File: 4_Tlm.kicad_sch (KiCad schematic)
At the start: 42 parts, among them J502 Conn_Coaxial, SW501 SW_Push, U501 W25Q128JVE, U502 RP2040, U503 Ra-08H

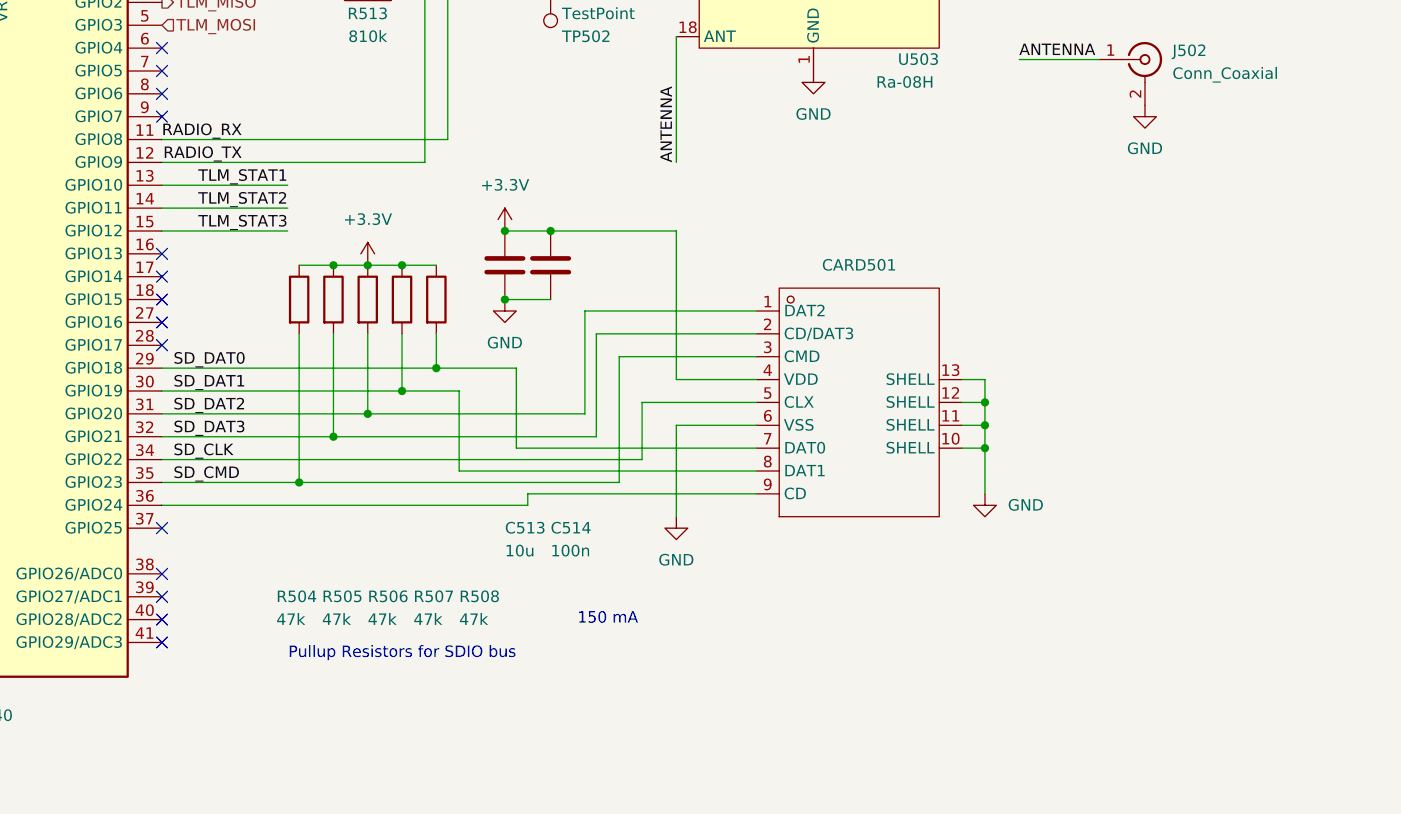
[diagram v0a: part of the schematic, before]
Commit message: Used a different microSD card slot symbol (The old one loooked bad)
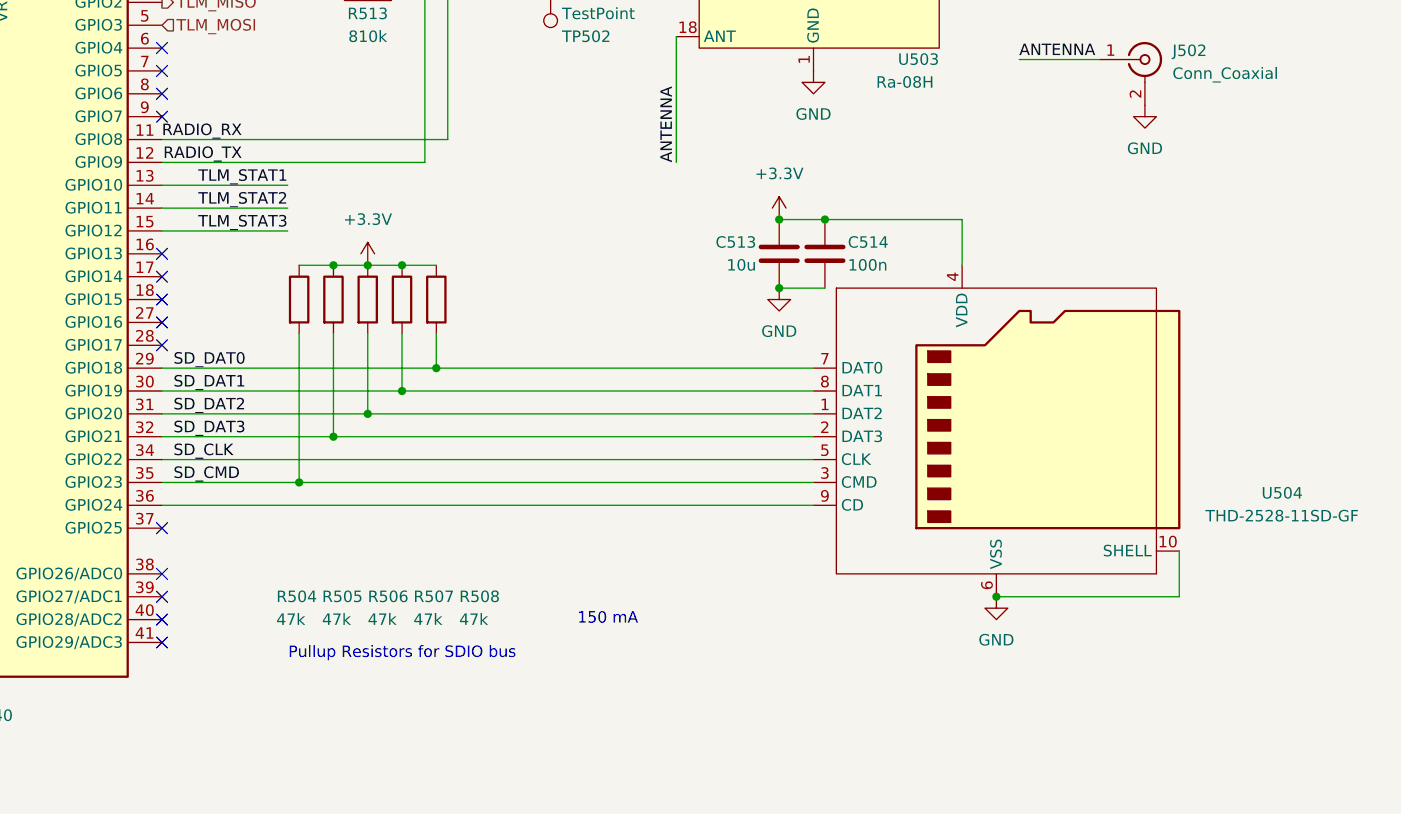
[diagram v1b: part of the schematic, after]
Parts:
- removed CARD501: (no value), Polaris:TF-SMD_THD2528-11SD-GF, symbol Polaris_symbols:THD2528-11SD-GF
- added U504: THD-2528-11SD-GF, Polaris:TF-SMD_THD2528-11SD-GF, symbol Polaris_symbols:MicroSD_THD2528-11SD-GF
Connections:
- net +3.3V: now also U504.4 (VDD)
- net GND: now also U504.10 (SHELL), U504.11 (SHELL), U504.12 (SHELL), U504.13 (SHELL), U504.6 (VSS)
- net SD_CLK: now also U504.5 (CLK)
- net SD_CMD: now also U504.3 (CMD)
- net SD_DAT0: now also U504.7 (DAT0)
- net SD_DAT1: now also U504.8 (DAT1)
- net SD_DAT2: now also U504.1 (DAT2)
- net SD_DAT3: now also U504.2 (DAT3)
- net at U502.36 (GPIO24): now also U504.9 (CD)
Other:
- moved on the sheet: C513, C514

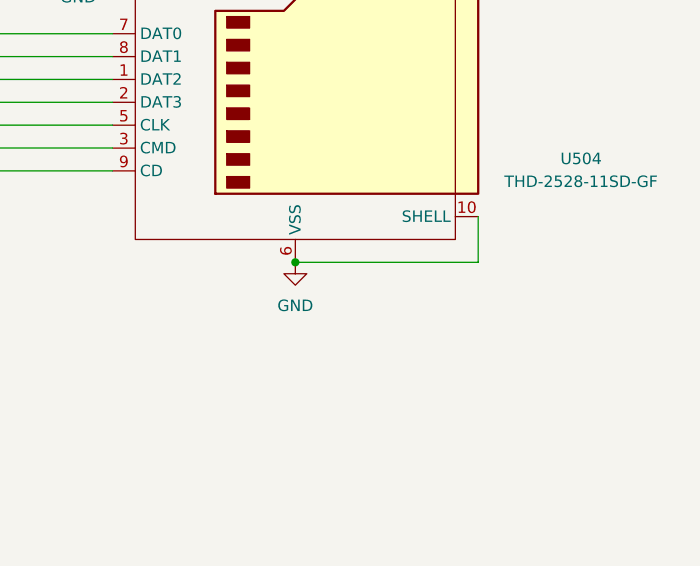
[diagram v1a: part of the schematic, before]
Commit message: Added hardware switch for active control Also added a coupling capacitor between receptacle shells and reference ground Added some more notes
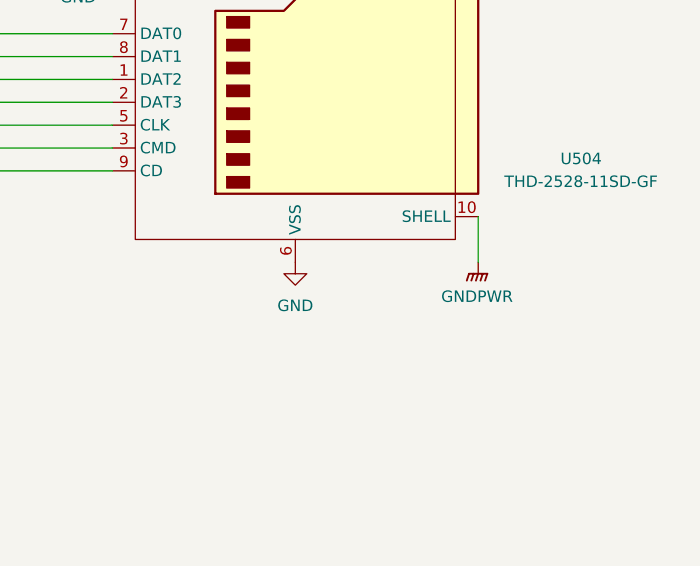
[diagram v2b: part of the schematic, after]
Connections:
- net GND: no longer U504.10 (SHELL), U504.11 (SHELL), U504.12 (SHELL), U504.13 (SHELL)
- new net GNDPWR: U504.10 (SHELL), U504.11 (SHELL), U504.12 (SHELL), U504.13 (SHELL)
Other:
- title: (none) -> Polaris/TLM
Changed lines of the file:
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@@
 	(generator_version "10.0")
 	(paper "A4")
+	(title_block
+		(title "Polaris/TLM")
+	)
 	(rectangle
 		(start 25.4 152.4)
@@
 	)
 	(junction
-		(at 251.46 158.75)
-		(diameter 0)
-		(color 0 0 0 0)
-	)
-	(junction
 		(at 171.45 60.96)
 		(diameter 0)
@@
 	(wire
 		(pts
-			(xy 271.78 153.67) (xy 271.78 158.75)
-		)
-		(stroke
-			(width 0)
-			(type default)
-		)
-	)
-	(wire
-		(pts
 			(xy 181.61 129.54) (xy 181.61 138.43)
 		)
@@
 	(wire
 		(pts
-			(xy 271.78 158.75) (xy 251.46 158.75)
+			(xy 232.41 116.84) (xy 247.65 116.84)
 		)
 		(stroke
@@
 	(wire
 		(pts
-			(xy 232.41 116.84) (xy 247.65 116.84)
+			(xy 177.8 129.54) (xy 177.8 140.97)
 		)
 		(stroke
@@
 	(wire
 		(pts
-			(xy 177.8 129.54) (xy 177.8 140.97)
+			(xy 171.45 60.96) (xy 179.07 60.96)
 		)
 		(stroke
@@
 	(wire
 		(pts
-			(xy 171.45 60.96) (xy 179.07 60.96)
+			(xy 95.25 110.49) (xy 100.33 110.49)
 		)
 		(stroke
@@
 	(wire
 		(pts
-			(xy 95.25 110.49) (xy 100.33 110.49)
+			(xy 177.8 140.97) (xy 231.14 140.97)
 		)
 		(stroke
@@
 	(wire
 		(pts
-			(xy 177.8 140.97) (xy 231.14 140.97)
+			(xy 53.34 130.81) (xy 107.95 130.81)
 		)
 		(stroke
@@
 	(wire
 		(pts
-			(xy 53.34 130.81) (xy 107.95 130.81)
+			(xy 53.34 133.35) (xy 107.95 133.35)
 		)
 		(stroke
@@
 	(wire
 		(pts
-			(xy 53.34 133.35) (xy 107.95 133.35)
+			(xy 271.78 153.67) (xy 271.78 158.75)
 		)
 		(stroke
@@
 					(unit 1)
 				)
+			)
+		)
+	)
+	(symbol
+		(lib_id "power:GNDPWR")
+		(at 271.78 158.75 0)
+		(unit 1)
+		(body_style 1)
+		(exclude_from_sim no)
+		(in_bom yes)
+		(on_board yes)
+		(in_pos_files yes)
+		(dnp no)
+		(fields_autoplaced yes)
+		(property "Reference" "#PWR0516"
+			(at 271.78 163.83 0)
+			(hide yes)
+			(show_name no)
+			(do_not_autoplace no)
+			(effects
+				(font
+					(size 1.27 1.27)
+				)
+			)
+		)
+		(property "Value" "GNDPWR"
+			(at 271.653 162.56 0)
+			(show_name no)
+			(do_not_autoplace no)
+			(effects
+				(font
+					(size 1.27 1.27)
+				)
+			)
+		)
+		(property "Footprint" ""
+			(at 271.78 160.02 0)
+			(hide yes)
+			(show_name no)
+			(do_not_autoplace no)
+			(effects
+				(font
+					(size 1.27 1.27)
+				)
+			)
+		)
+		(property "Datasheet" ""
+			(at 271.78 160.02 0)
+			(hide yes)
+			(show_name no)
+			(do_not_autoplace no)
+			(effects
+				(font
+					(size 1.27 1.27)
+				)
+			)
+		)
+		(property "Description" "Power symbol creates a global label with name \"GNDPWR\" , global ground"
+			(at 271.78 158.75 0)
+			(hide yes)
+			(show_name no)
+			(do_not_autoplace no)
+			(effects
+				(font
+					(size 1.27 1.27)
+				)
+			)
+		)
+		(pin "1"
+		)
+		(instances
+			(project "polaris"
+				(path "/cfb90e19-9fbe-47a1-a5ac-df522853d1d0/fe5e17e9-7440-4fbd-b2a1-319d9cc92848"
+					(reference "#PWR0516")
+					(unit 1)
+				)

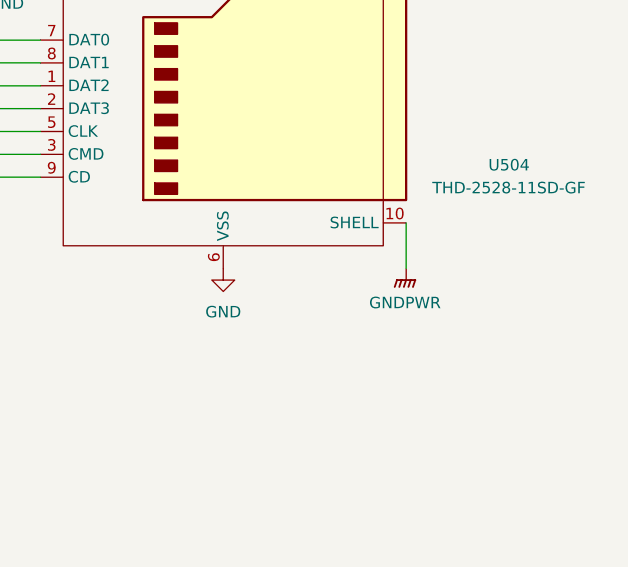
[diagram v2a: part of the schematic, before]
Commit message: Corrected grounding of shield pins in receptacles Also changed SHELL pin of microSD slot to Passive
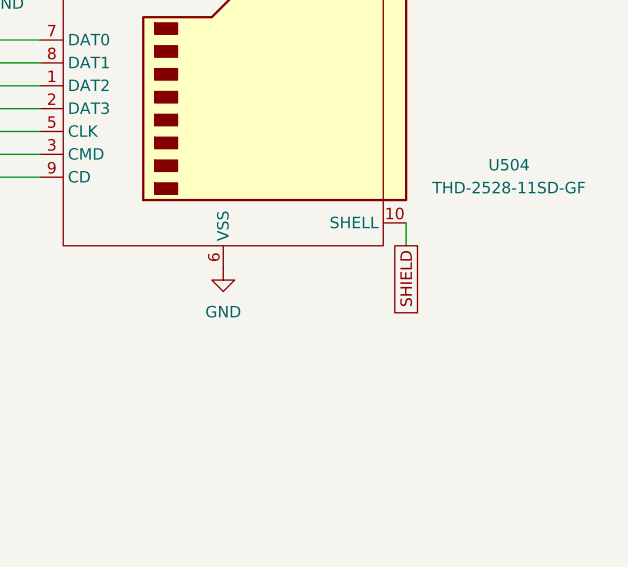
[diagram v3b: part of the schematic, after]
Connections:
- net GNDPWR renamed SHIELD
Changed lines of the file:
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@@
+	(wire
+		(pts
+			(xy 271.78 153.67) (xy 271.78 156.21)
+		)
+		(stroke
+			(width 0)
+			(type default)
+		)
+	)
 	(wire
 		(pts
@@
 	(wire
 		(pts
-			(xy 271.78 153.67) (xy 271.78 158.75)
+			(xy 130.81 74.93) (xy 130.81 80.01)
 		)
 		(stroke
@@
 	(wire
 		(pts
-			(xy 130.81 74.93) (xy 130.81 80.01)
+			(xy 135.89 74.93) (xy 130.81 74.93)
 		)
 		(stroke
@@
 	(wire
 		(pts
-			(xy 135.89 74.93) (xy 130.81 74.93)
+			(xy 160.02 60.96) (xy 171.45 60.96)
 		)
 		(stroke
@@
 	(wire
 		(pts
-			(xy 160.02 60.96) (xy 171.45 60.96)
+			(xy 190.5 76.2) (xy 190.5 107.95)
 		)
 		(stroke
@@
 	(wire
 		(pts
-			(xy 190.5 76.2) (xy 190.5 107.95)
+			(xy 257.81 68.58) (xy 266.7 68.58)
 		)
 		(stroke
@@
 	(wire
 		(pts
-			(xy 257.81 68.58) (xy 266.7 68.58)
+			(xy 158.75 138.43) (xy 181.61 138.43)
 		)
 		(stroke
@@
 	(wire
 		(pts
-			(xy 158.75 138.43) (xy 181.61 138.43)
+			(xy 66.04 71.12) (xy 74.93 71.12)
 		)
 		(stroke
@@
 	(wire
 		(pts
-			(xy 66.04 71.12) (xy 74.93 71.12)
+			(xy 231.14 60.96) (xy 233.68 60.96)
 		)
 		(stroke
@@
 	(wire
 		(pts
-			(xy 231.14 60.96) (xy 233.68 60.96)
+			(xy 57.15 160.02) (xy 60.96 160.02)
 		)
 		(stroke
@@
 	(wire
 		(pts
-			(xy 57.15 160.02) (xy 60.96 160.02)
+			(xy 158.75 118.11) (xy 172.72 118.11)
 		)
 		(stroke
@@
 	(wire
 		(pts
-			(xy 158.75 118.11) (xy 172.72 118.11)
+			(xy 146.05 69.85) (xy 146.05 60.96)
 		)
 		(stroke
@@
 	(wire
 		(pts
-			(xy 146.05 69.85) (xy 146.05 60.96)
+			(xy 185.42 135.89) (xy 231.14 135.89)
 		)
 		(stroke
@@
 		)
 	)
-	(wire
-		(pts
-			(xy 185.42 135.89) (xy 231.14 135.89)
-		)
-		(stroke
-			(width 0)
-			(type default)
-		)
-	)
 	(label "FLASH_IO3"
 		(at 53.34 133.35 0)
@@
 			)
 			(justify left bottom)
+		)
+	)
+	(global_label "SHIELD"
+		(shape passive)
+		(at 271.78 156.21 270)
+		(fields_autoplaced yes)
+		(effects
+			(font
+				(size 1.27 1.27)
+			)
+			(justify right)
+		)
+		(property "Intersheetrefs" "${INTERSHEET_REFS}"
+			(at 271.78 164.6758 90)
+			(hide yes)
+			(show_name no)
+			(do_not_autoplace no)
+			(effects
+				(font
+					(size 1.27 1.27)
+				)
+				(justify right)
+			)
 		)
 	)
@@
 					(unit 1)
 				)
-			)
-		)
-	)
-	(symbol
-		(lib_id "power:GNDPWR")
-		(at 271.78 158.75 0)
-		(unit 1)
-		(body_style 1)
-		(exclude_from_sim no)
-		(in_bom yes)
-		(on_board yes)
-		(in_pos_files yes)
-		(dnp no)
-		(fields_autoplaced yes)
-		(property "Reference" "#PWR0516"
-			(at 271.78 163.83 0)
-			(hide yes)
-			(show_name no)
-			(do_not_autoplace no)
-			(effects
-				(font
-					(size 1.27 1.27)
-				)
-			)
-		)
-		(property "Value" "GNDPWR"
-			(at 271.653 162.56 0)
-			(show_name no)
-			(do_not_autoplace no)
-			(effects
-				(font
-					(size 1.27 1.27)
-				)
-			)
-		)
-		(property "Footprint" ""
-			(at 271.78 160.02 0)
-			(hide yes)
-			(show_name no)
-			(do_not_autoplace no)
-			(effects
-				(font
-					(size 1.27 1.27)
-				)
-			)
-		)
-		(property "Datasheet" ""
-			(at 271.78 160.02 0)
-			(hide yes)
-			(show_name no)
-			(do_not_autoplace no)
-			(effects
-				(font
-					(size 1.27 1.27)
-				)
-			)
-		)
-		(property "Description" "Power symbol creates a global label with name \"GNDPWR\" , global ground"
-			(at 271.78 158.75 0)
-			(hide yes)
-			(show_name no)
-			(do_not_autoplace no)
-			(effects
-				(font
-					(size 1.27 1.27)
-				)
-			)
-		)
-		(pin "1"
-		)
-		(instances
-			(project "polaris"
-				(path "/cfb90e19-9fbe-47a1-a5ac-df522853d1d0/fe5e17e9-7440-4fbd-b2a1-319d9cc92848"
-					(reference "#PWR0516")
-					(unit 1)
-				)

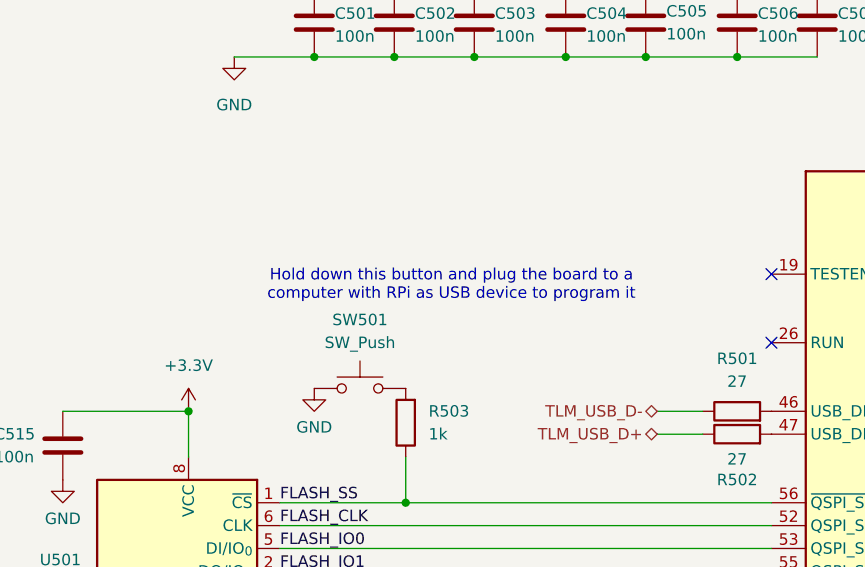
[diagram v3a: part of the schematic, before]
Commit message: Added more notes and finished footprint assignment
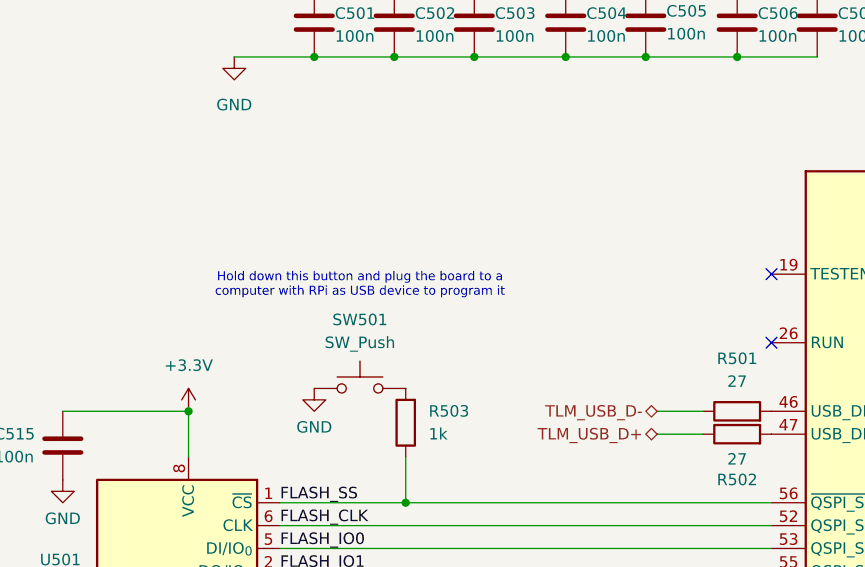
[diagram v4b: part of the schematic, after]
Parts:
- R512, R513: footprint (none) -> Resistor_SMD:R_0603_1608Metric

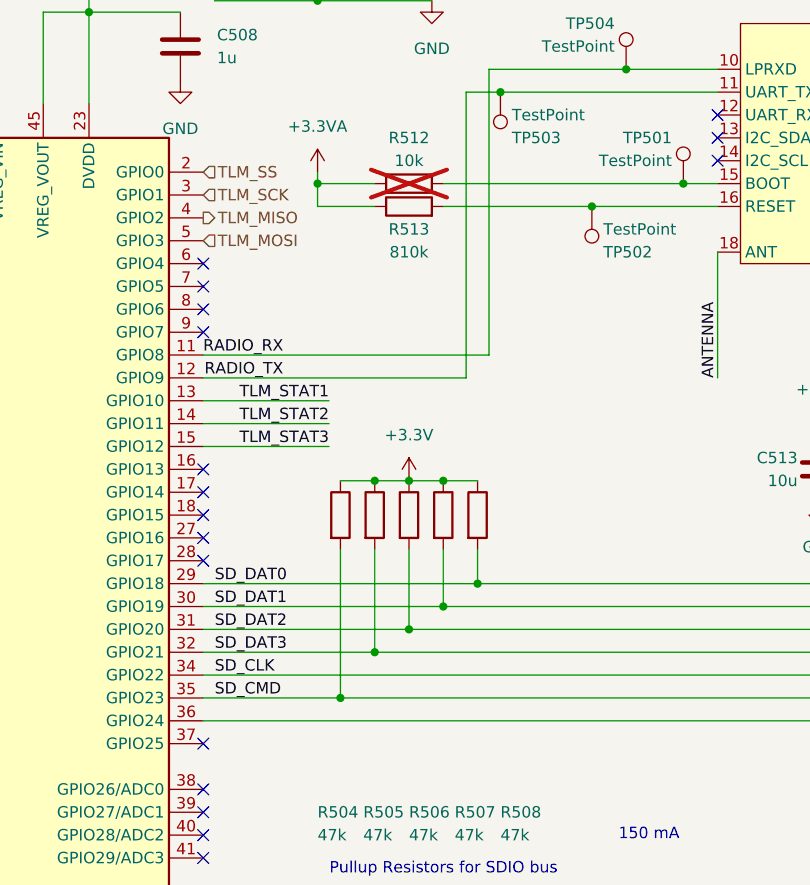
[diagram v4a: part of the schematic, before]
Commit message: Finally started the PCB layout and routing Only took me a few decades Also labeled some unlabeled nets in the schematic Changed the USB mux to be two 1x3 pin headers instead of one 2x3 Edited symbols and footprints to match pin numbers
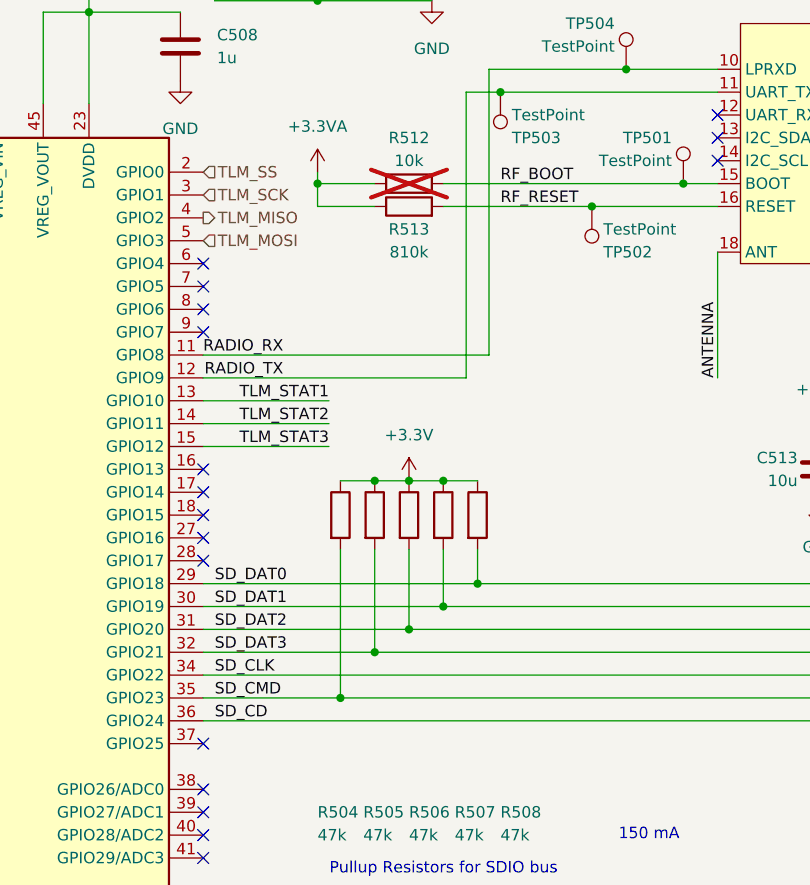
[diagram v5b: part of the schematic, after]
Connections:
- net SD_CD: now reaches U502.36 (GPIO24), U504.9 (CD)
- net RF_BOOT: now reaches R512.2, TP501.1, U503.15 (BOOT)
- net RF_RESET: now reaches R513.2, TP502.1, U503.16 (RESET)
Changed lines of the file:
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@@
+		)
+	)
+	(label "SD_CD"
+		(at 160.02 148.59 0)
+		(effects
+			(font
+				(size 1.27 1.27)
+			)
+			(justify left bottom)
 		)
 	)
@@
 		(effects
 			(font
+				(size 1.27 1.27)
+			)
+			(justify left bottom)
+		)
+	)
+	(label "RF_RESET"
+		(at 191.77 91.44 0)
+		(effects
+			(font
+				(size 1.27 1.27)
+			)
+			(justify left bottom)
+		)
+	)
+	(label "RF_BOOT"
+		(at 191.77 88.9 0)
+		(effects
+			(font
